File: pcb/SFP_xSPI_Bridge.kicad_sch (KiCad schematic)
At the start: 0 parts

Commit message: pcb: schemat - wersja robocza (FPGA, modul SFP, zlacza)
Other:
- added sheet EXT_IO (ext_io.kicad_sch)
- added sheet MISC (misc.kicad_sch)
- added sheet PWR (pwr.kicad_sch)
- added sheet SFP (sfp.kicad_sch)
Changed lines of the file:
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@@
 	(generator_version "10.0")
 	(paper "A4")
+	(sheet
+		(at 95.25 59.69)
+		(size 19.05 11.43)
+		(exclude_from_sim no)
+		(in_bom yes)
+		(on_board yes)
+		(dnp no)
+		(fields_autoplaced yes)
+		(stroke
+			(width 0.1524)
+			(type solid)
+		)
+		(fill
+			(color 0 0 0 0)
+		)
+		(property "Sheetname" "EXT_IO"
+			(at 95.25 58.9784 0)
+			(show_name no)
+			(do_not_autoplace no)
+			(effects
+				(font
+					(size 1.27 1.27)
+				)
+				(justify left bottom)
+			)
+		)
+		(property "Sheetfile" "ext_io.kicad_sch"
+			(at 95.25 71.7046 0)
+			(show_name no)
+			(do_not_autoplace no)
+			(effects
+				(font
+					(size 1.27 1.27)
+				)
+				(justify left top)
+			)
+		)
+		(instances
+			(project "SFP_xSPI_Bridge"
+				(path "/ca6491fd-e294-4986-aca7-b24059be2f57"
+					(page "4")
+				)
+			)
+		)
+	)
+	(sheet
+		(at 95.25 31.75)
+		(size 19.05 12.7)
+		(exclude_from_sim no)
+		(in_bom yes)
+		(on_board yes)
+		(dnp no)
+		(fields_autoplaced yes)
+		(stroke
+			(width 0.1524)
+			(type solid)
+		)
+		(fill
+			(color 0 0 0 0)
+		)
+		(property "Sheetname" "SFP"
+			(at 95.25 31.0384 0)
+			(show_name no)
+			(do_not_autoplace no)
+			(effects
+				(font
+					(size 1.27 1.27)
+				)
+				(justify left bottom)
+			)
+		)
+		(property "Sheetfile" "sfp.kicad_sch"
+			(at 95.25 45.0346 0)
+			(show_name no)
+			(do_not_autoplace no)
+			(effects
+				(font
+					(size 1.27 1.27)
+				)
+				(justify left top)
+			)
+		)
+		(instances
+			(project "SFP_xSPI_Bridge"
+				(path "/ca6491fd-e294-4986-aca7-b24059be2f57"
+					(page "2")
+				)
+			)
+		)
+	)
+	(sheet
+		(at 137.16 59.69)
+		(size 19.05 11.43)
+		(exclude_from_sim no)
+		(in_bom yes)
+		(on_board yes)
+		(dnp no)
+		(fields_autoplaced yes)
+		(stroke
+			(width 0.1524)
+			(type solid)
+		)
+		(fill
+			(color 0 0 0 0)
+		)
+		(property "Sheetname" "MISC"
+			(at 137.16 58.9784 0)
+			(show_name no)
+			(do_not_autoplace no)
+			(effects
+				(font
+					(size 1.27 1.27)
+				)
+				(justify left bottom)
+			)
+		)
+		(property "Sheetfile" "misc.kicad_sch"
+			(at 137.16 71.7046 0)
+			(show_name no)
+			(do_not_autoplace no)
+			(effects
+				(font
+					(size 1.27 1.27)
+				)
+				(justify left top)
+			)
+		)
+		(instances
+			(project "SFP_xSPI_Bridge"
+				(path "/ca6491fd-e294-4986-aca7-b24059be2f57"
+					(page "5")
+				)
+			)
+		)
+	)
+	(sheet
+		(at 137.16 31.75)
+		(size 19.05 10.16)
+		(exclude_from_sim no)
+		(in_bom yes)
+		(on_board yes)
+		(dnp no)
+		(fields_autoplaced yes)
+		(stroke
+			(width 0.1524)
+			(type solid)
+		)
+		(fill
+			(color 0 0 0 0)
+		)
+		(property "Sheetname" "PWR"
+			(at 137.16 31.0384 0)
+			(show_name no)
+			(do_not_autoplace no)
+			(effects
+				(font
+					(size 1.27 1.27)
+				)
+				(justify left bottom)
+			)
+		)
+		(property "Sheetfile" "pwr.kicad_sch"
+			(at 137.16 42.4946 0)
+			(show_name no)
+			(do_not_autoplace no)
+			(effects
+				(font
+					(size 1.27 1.27)
+				)
+				(justify left top)
+			)
+		)
+		(instances
+			(project "SFP_xSPI_Bridge"
+				(path "/ca6491fd-e294-4986-aca7-b24059be2f57"
+					(page "3")
+				)
+			)
+		)
+	)
 	(sheet_instances
 		(path "/"

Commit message: pcb: schemat rev. A
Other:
- removed sheet MISC
- sheet EXT_IO ports: added SFP_SCL, SFP_SDA; removed none
- sheet SFP ports: added SFP_SCL, SFP_SDA; removed none
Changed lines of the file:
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@@
 	(generator_version "10.0")
 	(paper "A4")
+	(wire
+		(pts
+			(xy 114.3 40.64) (xy 135.89 40.64)
+		)
+		(stroke
+			(width 0)
+			(type default)
+		)
+	)
+	(wire
+		(pts
+			(xy 114.3 38.1) (xy 135.89 38.1)
+		)
+		(stroke
+			(width 0)
+			(type default)
+		)
+	)
 	(sheet
-		(at 95.25 59.69)
+		(at 135.89 33.02)
 		(size 19.05 11.43)
 		(exclude_from_sim no)
@@
 		)
 		(property "Sheetname" "EXT_IO"
-			(at 95.25 58.9784 0)
+			(at 135.89 32.3084 0)
 			(show_name no)
 			(do_not_autoplace no)
@@
 		)
 		(property "Sheetfile" "ext_io.kicad_sch"
-			(at 95.25 71.7046 0)
+			(at 135.89 45.0346 0)
 			(show_name no)
 			(do_not_autoplace no)
@@
 				)
 				(justify left top)
+			)
+		)
+		(pin "SFP_SCL" input
+			(at 135.89 40.64 180)
+			(effects
+				(font
+					(size 1.27 1.27)
+				)
+				(justify left)
+			)
+		)
+		(pin "SFP_SDA" input
+			(at 135.89 38.1 180)
+			(effects
+				(font
+					(size 1.27 1.27)
+				)
+				(justify left)
 			)
 		)
@@
 	)
 	(sheet
-		(at 95.25 31.75)
-		(size 19.05 12.7)
+		(at 95.25 33.02)
+		(size 19.05 11.43)
 		(exclude_from_sim no)
 		(in_bom yes)
@@
 		)
 		(property "Sheetname" "SFP"
-			(at 95.25 31.0384 0)
+			(at 95.25 32.3084 0)
 			(show_name no)
 			(do_not_autoplace no)
@@
 			)
 		)
+		(pin "SFP_SCL" input
+			(at 114.3 40.64 0)
+			(effects
+				(font
+					(size 1.27 1.27)
+				)
+				(justify right)
+			)
+		)
+		(pin "SFP_SDA" input
+			(at 114.3 38.1 0)
+			(effects
+				(font
+					(size 1.27 1.27)
+				)
+				(justify right)
+			)
+		)
 		(instances
 			(project "SFP_xSPI_Bridge"
@@
 	)
 	(sheet
-		(at 137.16 59.69)
-		(size 19.05 11.43)
-		(exclude_from_sim no)
-		(in_bom yes)
-		(on_board yes)
-		(dnp no)
-		(fields_autoplaced yes)
-		(stroke
-			(width 0.1524)
-			(type solid)
-		)
-		(fill
-			(color 0 0 0 0)
-		)
-		(property "Sheetname" "MISC"
-			(at 137.16 58.9784 0)
-			(show_name no)
-			(do_not_autoplace no)
-			(effects
-				(font
-					(size 1.27 1.27)
-				)
-				(justify left bottom)
-			)
-		)
-		(property "Sheetfile" "misc.kicad_sch"
-			(at 137.16 71.7046 0)
-			(show_name no)
-			(do_not_autoplace no)
-			(effects
-				(font
-					(size 1.27 1.27)
-				)
-				(justify left top)
-			)
-		)
-		(instances
-			(project "SFP_xSPI_Bridge"
-				(path "/ca6491fd-e294-4986-aca7-b24059be2f57"
-					(page "5")
-				)
-			)
-		)
-	)
-	(sheet
-		(at 137.16 31.75)
+		(at 96.52 59.69)
 		(size 19.05 10.16)
 		(exclude_from_sim no)
@@
 		)
 		(property "Sheetname" "PWR"
-			(at 137.16 31.0384 0)
+			(at 96.52 58.9784 0)
 			(show_name no)
 			(do_not_autoplace no)
@@
 		)
 		(property "Sheetfile" "pwr.kicad_sch"
-			(at 137.16 42.4946 0)
+			(at 96.52 70.4346 0)
 			(show_name no)
 			(do_not_autoplace no)

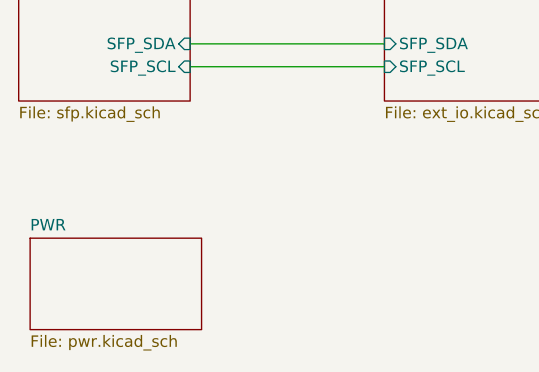
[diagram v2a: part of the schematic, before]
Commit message: pcb: rozmieszczenie i czesc routingu, odwrocona para RD, reguly i klasy sieci
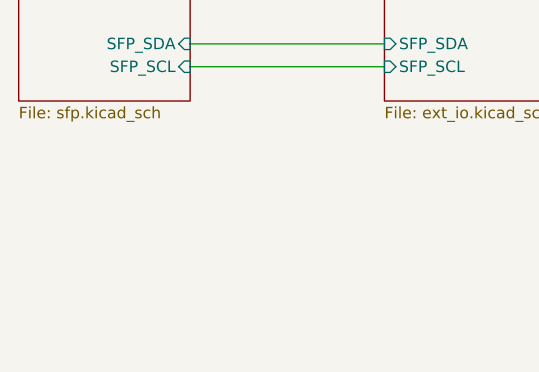
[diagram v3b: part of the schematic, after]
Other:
- removed sheet PWR
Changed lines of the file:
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@@
-		)
-	)
-	(sheet
-		(at 96.52 59.69)
-		(size 19.05 10.16)
-		(exclude_from_sim no)
-		(in_bom yes)
-		(on_board yes)
-		(dnp no)
-		(fields_autoplaced yes)
-		(stroke
-			(width 0.1524)
-			(type solid)
-		)
-		(fill
-			(color 0 0 0 0)
-		)
-		(property "Sheetname" "PWR"
-			(at 96.52 58.9784 0)
-			(show_name no)
-			(do_not_autoplace no)
-			(effects
-				(font
-					(size 1.27 1.27)
-				)
-				(justify left bottom)
-			)
-		)
-		(property "Sheetfile" "pwr.kicad_sch"
-			(at 96.52 70.4346 0)
-			(show_name no)
-			(do_not_autoplace no)
-			(effects
-				(font
-					(size 1.27 1.27)
-				)
-				(justify left top)
-			)
-		)
-		(instances
-			(project "SFP_xSPI_Bridge"
-				(path "/ca6491fd-e294-4986-aca7-b24059be2f57"
-					(page "3")
-				)
-			)
 		)
 	)

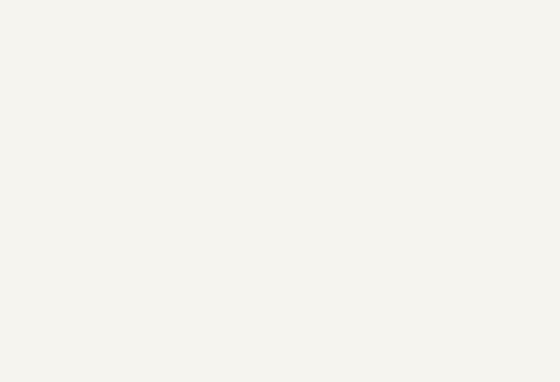
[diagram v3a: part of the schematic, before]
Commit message: pcb: otwory montazowe, zakonczenie routingu rev. A
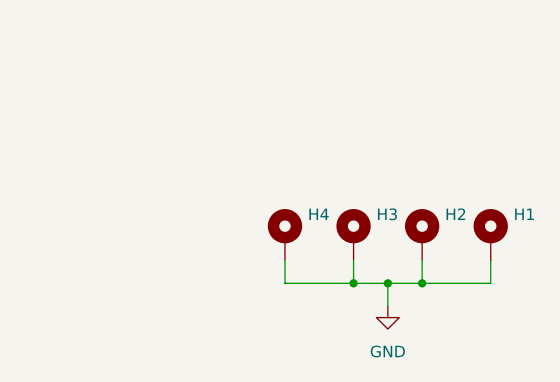
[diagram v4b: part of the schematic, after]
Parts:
- added H1, H2, H3, H4: MountingHole_Pad, MountingHole:MountingHole_2.7mm_M2.5_DIN965_Pad, symbol Mechanical:MountingHole_Pad
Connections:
- new net GND: H1.1, H2.1, H3.1, H4.1

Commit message: pcb: rev. A - obrys, strefy, pull-up SFP_TX_DIS, via stitching, usuniete puste arkusze; pliki produkcyjne: gerbery (zip), PDF schematu i PCB, iBOM, rendery 3D
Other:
- company: (none) -> bartkepl
- title: (none) -> SFP_xSPI_Bridge
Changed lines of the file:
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@@
 	(generator_version "10.0")
 	(paper "A4")
+	(title_block
+		(title "SFP_xSPI_Bridge")
+		(date "2026-10-09")
+		(rev "A")
+		(company "bartkepl")
+	)
 	(junction
 		(at 160.02 177.8)
